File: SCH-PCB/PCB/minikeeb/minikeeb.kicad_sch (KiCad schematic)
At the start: 90 parts, among them J1 OLED, SW10 SW_PUSH-Lily58-cache, SW11 SW_PUSH-Lily58-cache, SW12 SW_PUSH-Lily58-cache, SW13 SW_PUSH-Lily58-cache, SW14 SW_PUSH-Lily58-cache, SW15 SW_PUSH-Lily58-cache, SW16 SW_PUSH-Lily58-cache, SW17 SW_PUSH-Lily58-cache, SW18 SW_PUSH-Lily58-cache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

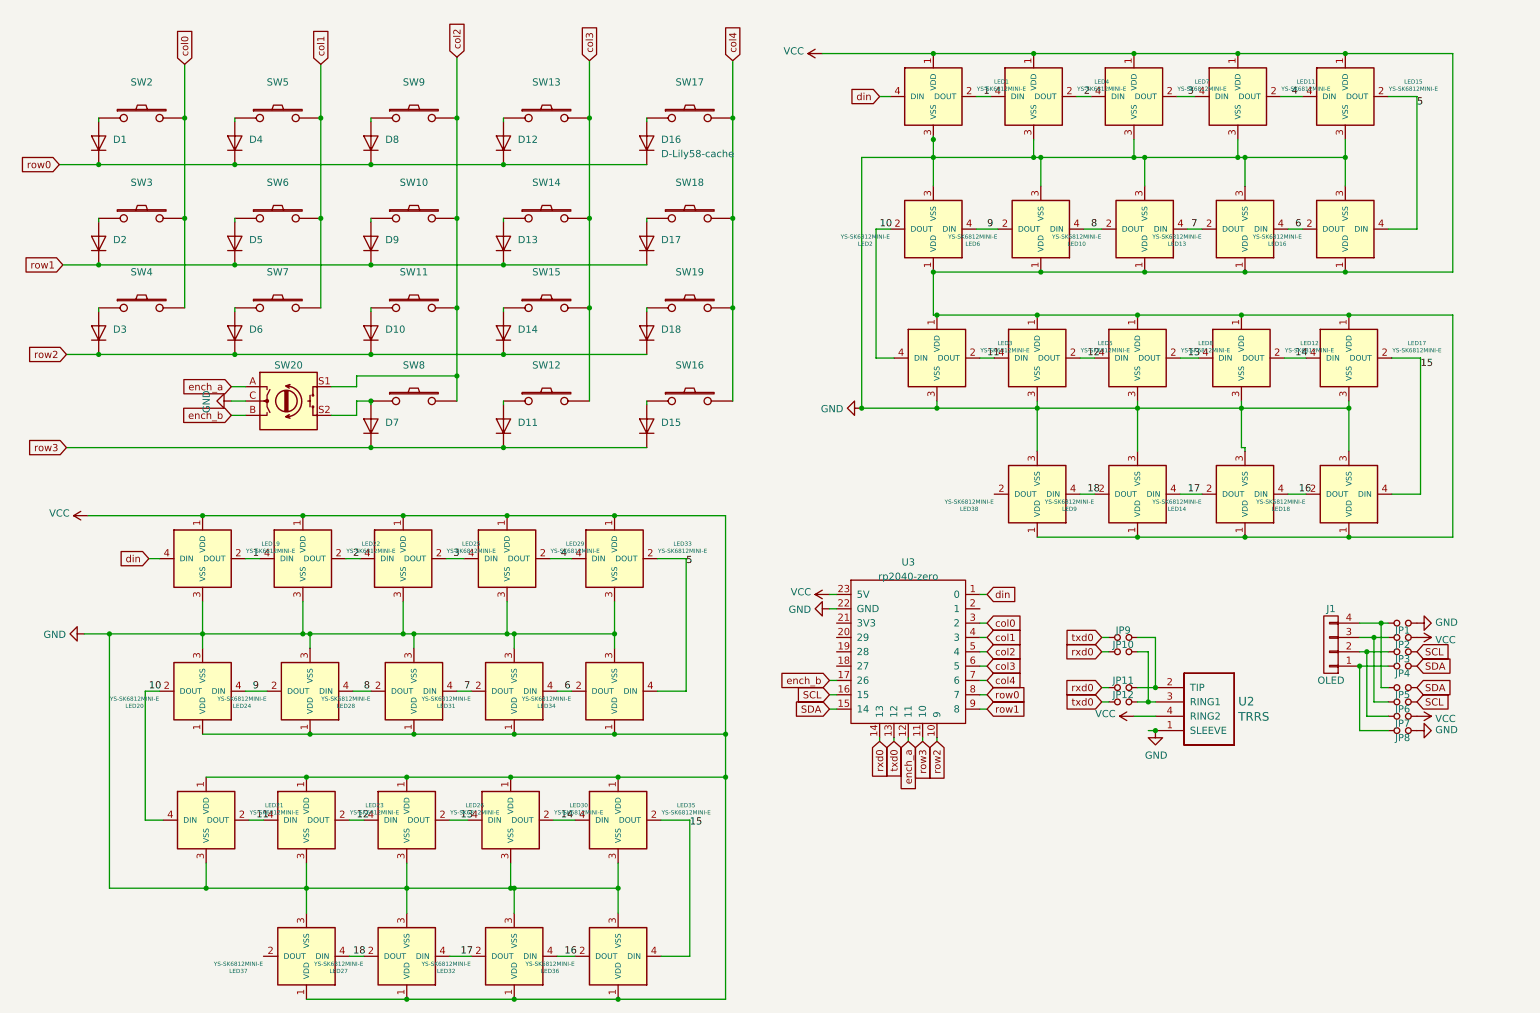
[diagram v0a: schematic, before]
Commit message: FEAT: change microcontroller to promicro layout
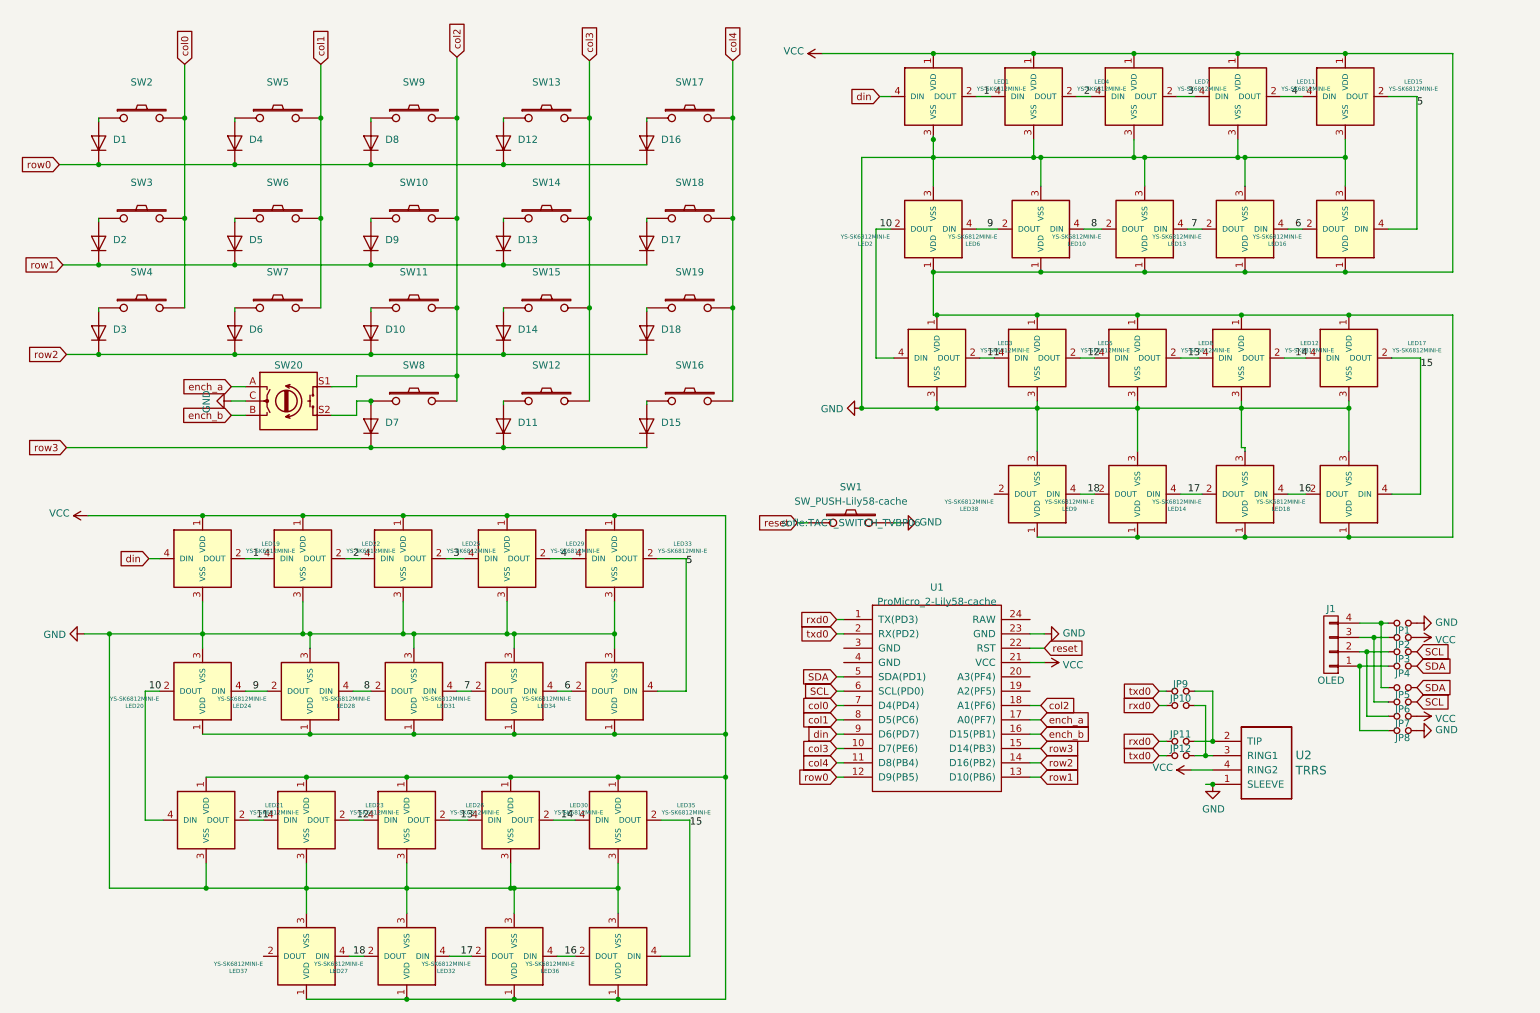
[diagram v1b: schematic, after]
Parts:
- removed U3: rp2040-zero, keeb_mcu:rp2040-zero-tht, symbol mcu_keeb:rp2040-zero
- added SW1: SW_PUSH-Lily58-cache, sofle:TACT_SWITCH_TVBP06, symbol sofle:SW_PUSH-Lily58-cache
- added U1: ProMicro_2-Lily58-cache, sofle:ArduinoProMicro-ZigZag-DoubleSided, symbol sofle:ProMicro_2-Lily58-cache
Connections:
- net GND: now also SW1.2, U1.23 (GND)
- net SCL: now also U1.6 (SCL(PD0))
- net SDA: now also U1.5 (SDA(PD1))
- net VCC: now also U1.21 (VCC)
- net col0: now also U1.7 (D4(PD4))
- net col1: now also U1.8 (D5(PC6))
- net col2: now also U1.18 (A1(PF6))
- net col3: now also U1.10 (D7(PE6))
- net col4: now also U1.11 (D8(PB4))
- net din: now also U1.9 (D6(PD7))
- net ench_a: now also U1.17 (A0(PF7))
- net ench_b: now also U1.16 (D15(PB1))
- net row0: now also U1.12 (D9(PB5))
- net row1: now also U1.13 (D10(PB6))
- net row2: now also U1.14 (D16(PB2))
- net row3: now also U1.15 (D14(PB3))
- net rxd0: now also U1.1 (TX(PD3))
- net txd0: now also U1.2 (RX(PD2))
- new net reset: SW1.1, U1.22 (RST)
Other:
- moved on the sheet: JP10, JP11, JP12, JP9, U2

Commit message: FEAT: update pcb
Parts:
- added J2, J3: Conn_01x02_Pin, Connector_JST:JST_EH_B2B-EH-A_1x02_P2.50mm_Vertical, symbol Connector:Conn_01x02_Pin
- added S1: JS102011SAQN, other:SW_JS102011SAQN, symbol other:JS102011SAQN
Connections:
- new net: J3.1 (Pin_1), S1.2
- new net: J2.2 (Pin_2), J3.2 (Pin_2)
- new net: J2.1 (Pin_1), S1.1
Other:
- moved on the sheet: J1, JP1, JP2, JP3, JP4, JP5, JP6, JP7, JP8

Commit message: FEAT: update pcb for vcc selection
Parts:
- added JP13, JP14: Jumper_NO_Small, sofle:Jumper, symbol SofleKeyboard-rescue:Jumper_NO_Small-Device
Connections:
- net VCC: now also JP13.1, JP14.1; no longer U1.21 (VCC)
- net at U1.24 (RAW): now also JP13.2
- new net: JP14.2, U1.21 (VCC)
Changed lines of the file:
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@@
   (junction (at 100.965 53.975) (diameter 0) (color 0 0 0 0)
   )
+  (junction (at 223.52 132.715) (diameter 0) (color 0 0 0 0)
+  )
   (junction (at 234.95 154.305) (diameter 0) (color 0 0 0 0)
   )
@@
     (stroke (width 0) (type default))
   )
+  (wire (pts (xy 223.52 132.715) (xy 225.425 132.715))
+    (stroke (width 0) (type default))
+  )
   (wire (pts (xy 264.795 144.145) (xy 264.795 155.575))
     (stroke (width 0) (type default))
@@
     (stroke (width 0) (type default))
   )
+  (wire (pts (xy 202.565 132.715) (xy 218.44 132.715))
+    (stroke (width 0) (type default))
+  )
   (wire (pts (xy 141.605 114.3) (xy 141.605 137.795))
     (stroke (width 0) (type default))
@@
     (stroke (width 0) (type default))
   )
+  (wire (pts (xy 223.52 125.095) (xy 223.52 132.715))
+    (stroke (width 0) (type default))
+  )
   (wire (pts (xy 111.125 127.635) (xy 111.125 130.175))
     (stroke (width 0) (type default))
@@
     (stroke (width 0) (type default))
   )
+  (wire (pts (xy 202.565 125.095) (xy 218.44 125.095))
+    (stroke (width 0) (type default))
+  )
   (wire (pts (xy 91.44 106.68) (xy 109.855 106.68))
     (stroke (width 0) (type default))
@@
     (stroke (width 0) (type default))
   )
-  (wire (pts (xy 202.565 132.715) (xy 205.105 132.715))
-    (stroke (width 0) (type default))
-  )
   (wire (pts (xy 271.145 32.385) (xy 271.145 55.88))
     (stroke (width 0) (type default))
@@
     )
   )
+  (symbol (lib_id "SofleKeyboard-rescue:Jumper_NO_Small-Device") (at 220.98 125.095 180) (unit 1)
+    (in_bom yes) (on_board yes) (dnp no)
+    (property "Reference" "JP13" (at 220.98 123.825 0)
+      (effects (font (size 1.27 1.27)))
+    )
+    (property "Value" "Jumper_NO_Small" (at 220.98 127.4826 0)
+      (effects (font (size 1.27 1.27)) hide)
+    )
+    (property "Footprint" "sofle:Jumper" (at 220.98 125.095 0)
+      (effects (font (size 1.27 1.27)) hide)
+    )
+    (property "Datasheet" "~" (at 220.98 125.095 0)
+      (effects (font (size 1.27 1.27)) hide)
+    )
+    (pin "1")
+    (pin "2")
+    (instances
+      (project "minikeeb"
+        (path "/2d29fb35-10cd-40a1-be26-d1c36146b851"
+          (reference "JP13") (unit 1)
+        )
+      )
+      (project "SofleKeyboard"
+        (path "/aece9479-71e1-49b1-8c05-47c45eafcac9"
+          (reference "JP8") (unit 1)
+        )
+      )
+    )
+  )
   (symbol (lib_id "kbd:YS-SK6812MINI-E") (at 74.295 184.785 180) (unit 1)
     (in_bom yes) (on_board yes) (dnp no) (fields_autoplaced)
@@
     )
   )
+  (symbol (lib_id "SofleKeyboard-rescue:Jumper_NO_Small-Device") (at 220.98 132.715 180) (unit 1)
+    (in_bom yes) (on_board yes) (dnp no)
+    (property "Reference" "JP14" (at 220.98 131.445 0)
+      (effects (font (size 1.27 1.27)))
+    )
+    (property "Value" "Jumper_NO_Small" (at 220.98 135.1026 0)
+      (effects (font (size 1.27 1.27)) hide)
+    )
+    (property "Footprint" "sofle:Jumper" (at 220.98 132.715 0)
+      (effects (font (size 1.27 1.27)) hide)
+    )
+    (property "Datasheet" "~" (at 220.98 132.715 0)
+      (effects (font (size 1.27 1.27)) hide)
+    )
+    (pin "1")
+    (pin "2")
+    (instances
+      (project "minikeeb"
+        (path "/2d29fb35-10cd-40a1-be26-d1c36146b851"
+          (reference "JP14") (unit 1)
+        )
+      )
+      (project "SofleKeyboard"
+        (path "/aece9479-71e1-49b1-8c05-47c45eafcac9"
+          (reference "JP8") (unit 1)
+        )
+      )
+    )
+  )
   (symbol (lib_id "sofle:SW_PUSH-Lily58-cache") (at 45.085 69.85 0) (unit 1)
     (in_bom yes) (on_board yes) (dnp no) (fields_autoplaced)
@@
     )
   )
-  (symbol (lib_id "power:VCC") (at 205.105 132.715 270) (unit 1)
+  (symbol (lib_id "power:VCC") (at 225.425 132.715 270) (unit 1)
     (in_bom yes) (on_board yes) (dnp no)
-    (property "Reference" "#PWR013" (at 201.295 132.715 0)
+    (property "Reference" "#PWR013" (at 221.615 132.715 0)
       (effects (font (size 1.27 1.27)) hide)
     )
-    (property "Value" "VCC" (at 208.3562 133.1468 90)
+    (property "Value" "VCC" (at 228.6762 133.1468 90)
       (effects (font (size 1.27 1.27)) (justify left))
     )
-    (property "Footprint" "" (at 205.105 132.715 0)
+    (property "Footprint" "" (at 225.425 132.715 0)
       (effects (font (size 1.27 1.27)) hide)
     )
-    (property "Datasheet" "" (at 205.105 132.715 0)
+    (property "Datasheet" "" (at 225.425 132.715 0)
       (effects (font (size 1.27 1.27)) hide)
     )
